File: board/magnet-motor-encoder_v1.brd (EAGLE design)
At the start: 22 x 22 mm, 14 parts, among them IC1 AS5045B, IC3 DS18B20

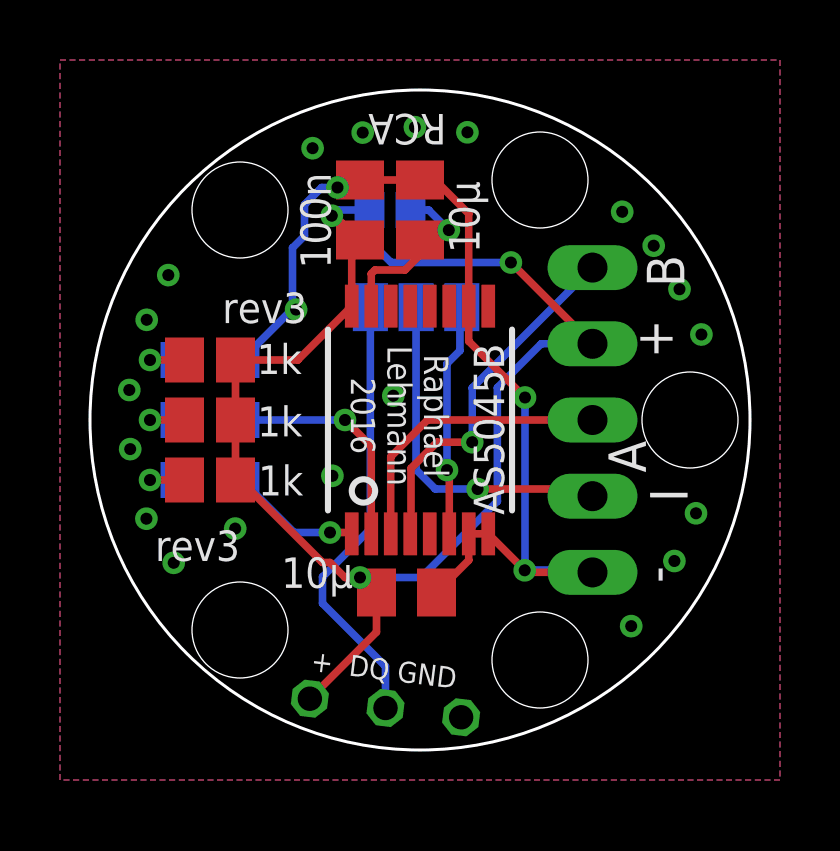
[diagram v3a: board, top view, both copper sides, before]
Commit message: board as5045b: integrate mounting holes in board outline
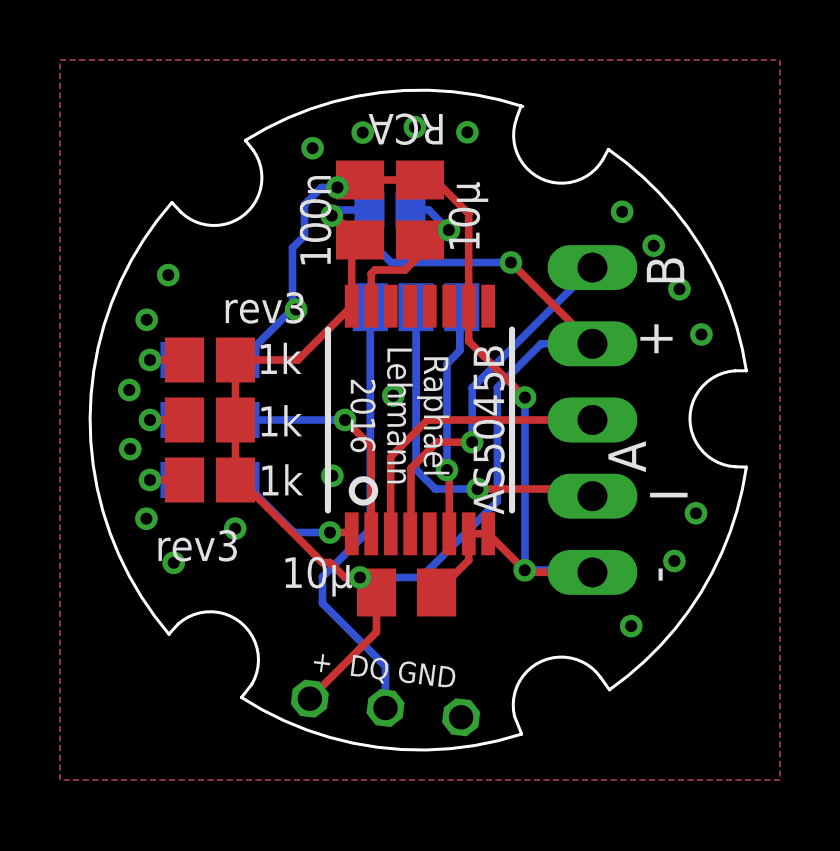
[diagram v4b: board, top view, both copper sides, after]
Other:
- board size 22 x 22 mm -> 21.9 x 22 mm
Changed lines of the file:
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@@
 <grid distance="0.01" unitdist="mm" unit="mm" style="dots" multiple="1" display="yes" altdistance="0.02" altunitdist="mm" altunit="mm"/>
 <layers>
-<layer number="1" name="Top" color="4" fill="1" visible="no" active="yes"/>
+<layer number="1" name="Top" color="4" fill="1" visible="yes" active="yes"/>
 <layer number="2" name="Route2" color="1" fill="3" visible="no" active="no"/>
 <layer number="3" name="Route3" color="4" fill="3" visible="no" active="no"/>
@@
 <layer number="19" name="Unrouted" color="6" fill="1" visible="yes" active="yes"/>
 <layer number="20" name="Dimension" color="15" fill="1" visible="yes" active="yes"/>
-<layer number="21" name="tPlace" color="7" fill="1" visible="no" active="yes"/>
+<layer number="21" name="tPlace" color="7" fill="1" visible="yes" active="yes"/>
 <layer number="22" name="bPlace" color="7" fill="1" visible="yes" active="yes"/>
-<layer number="23" name="tOrigins" color="15" fill="1" visible="no" active="yes"/>
+<layer number="23" name="tOrigins" color="15" fill="1" visible="yes" active="yes"/>
 <layer number="24" name="bOrigins" color="15" fill="1" visible="yes" active="yes"/>
 <layer number="25" name="tNames" color="7" fill="1" visible="no" active="yes"/>
-<layer number="26" name="bNames" color="7" fill="1" visible="yes" active="yes"/>
+<layer number="26" name="bNames" color="7" fill="1" visible="no" active="yes"/>
 <layer number="27" name="tValues" color="7" fill="1" visible="no" active="yes"/>
-<layer number="28" name="bValues" color="7" fill="1" visible="yes" active="yes"/>
+<layer number="28" name="bValues" color="7" fill="1" visible="no" active="yes"/>
 <layer number="29" name="tStop" color="7" fill="3" visible="no" active="yes"/>
 <layer number="30" name="bStop" color="7" fill="6" visible="no" active="yes"/>
@@
 <layer number="41" name="tRestrict" color="4" fill="10" visible="no" active="yes"/>
 <layer number="42" name="bRestrict" color="1" fill="10" visible="no" active="yes"/>
-<layer number="43" name="vRestrict" color="2" fill="10" visible="no" active="yes"/>
+<layer number="43" name="vRestrict" color="2" fill="10" visible="yes" active="yes"/>
 <layer number="44" name="Drills" color="7" fill="1" visible="no" active="yes"/>
-<layer number="45" name="Holes" color="7" fill="1" visible="no" active="yes"/>
-<layer number="46" name="Milling" color="3" fill="1" visible="no" active="yes"/>
-<layer number="47" name="Measures" color="7" fill="1" visible="no" active="yes"/>
-<layer number="48" name="Document" color="7" fill="1" visible="no" active="yes"/>
-<layer number="49" name="Reference" color="7" fill="1" visible="no" active="yes"/>
+<layer number="45" name="Holes" color="7" fill="1" visible="yes" active="yes"/>
+<layer number="46" name="Milling" color="3" fill="1" visible="yes" active="yes"/>
+<layer number="47" name="Measures" color="7" fill="1" visible="yes" active="yes"/>
+<layer number="48" name="Document" color="7" fill="1" visible="yes" active="yes"/>
+<layer number="49" name="Reference" color="7" fill="1" visible="yes" active="yes"/>
 <layer number="50" name="dxf" color="7" fill="1" visible="no" active="no"/>
 <layer number="51" name="tDocu" color="7" fill="1" visible="no" active="yes"/>
@@
 <board>
 <plain>
-<circle x="0" y="0" radius="11" width="0.1" layer="20"/>
-<hole x="-6" y="-7" drill="3.2"/>
-<hole x="4" y="-8" drill="3.2"/>
-<hole x="9" y="0" drill="3.2"/>
-<hole x="-6" y="7" drill="3.2"/>
-<hole x="4" y="8" drill="3.2"/>
 <text x="1.52" y="7.96" size="0.8128" layer="26" rot="MR0">Solder 3V</text>
 <text x="1.14" y="1.65" size="0.9" layer="26" rot="SMR270">LEDs 2mA</text>
@@
 <text x="-4.61" y="3.98" size="1.016" layer="26" ratio="15" distance="44" rot="MR0">rev3</text>
 <text x="-3.66" y="-8.36" size="0.7" layer="25" font="vector" rot="SR353">+  DQ GND</text>
+<wire x1="-5.82" y1="9.32" x2="3.43" y2="10.45" width="0.1" layer="20" curve="-50.215193"/>
+<wire x1="10.88" y1="1.64" x2="6.28" y2="9.02" width="0.1" layer="20" curve="46.611973"/>
+<wire x1="10.88" y1="-1.57" x2="6.32" y2="-8.99" width="0.1" layer="20" curve="-46.681469"/>
+<wire x1="3.39" y1="-10.47" x2="-5.95" y2="-9.25" width="0.1" layer="20" curve="-50.641989"/>
+<wire x1="-8.36" y1="-7.15" x2="-8.27" y2="7.25" width="0.1" layer="20" curve="-81.710622"/>
+<wire x1="-8.37" y1="-7.14" x2="-8.05" y2="-6.79" width="0.1" layer="20"/>
+<wire x1="-5.6" y1="-8.8" x2="-8.06" y2="-6.8" width="0.1" layer="20" curve="161.917892"/>
+<wire x1="3.15" y1="-9.87" x2="6.02" y2="-8.58" width="0.1" layer="20" curve="-157.942671"/>
+<wire x1="10.51" y1="1.64" x2="10.53" y2="-1.56" width="0.1" layer="20" curve="174.275412"/>
+<wire x1="3.21" y1="10.02" x2="6.09" y2="8.67" width="0.1" layer="20" curve="168.438521"/>
+<wire x1="-5.55" y1="8.98" x2="-7.97" y2="6.93" width="0.1" layer="20" curve="-168.517767"/>
+<wire x1="-5.95" y1="-9.25" x2="-5.6" y2="-8.8" width="0.1" layer="20"/>
+<wire x1="-8.27" y1="7.25" x2="-7.97" y2="6.93" width="0.1" layer="20"/>
+<wire x1="-5.82" y1="9.32" x2="-5.55" y2="8.98" width="0.1" layer="20"/>
+<wire x1="3.21" y1="10.03" x2="3.37" y2="10.47" width="0.1" layer="20"/>
+<wire x1="6.09" y1="8.67" x2="6.28" y2="9.02" width="0.1" layer="20"/>
+<wire x1="10.51" y1="1.64" x2="10.88" y2="1.64" width="0.1" layer="20"/>
+<wire x1="10.88" y1="-1.57" x2="10.53" y2="-1.56" width="0.1" layer="20"/>
+<wire x1="6.32" y1="-9" x2="6.02" y2="-8.58" width="0.1" layer="20"/>
+<wire x1="3.15" y1="-9.87" x2="3.39" y2="-10.47" width="0.1" layer="20"/>
 </plain>
 <attributes>
